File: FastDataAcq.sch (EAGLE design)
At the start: 223 parts, among them IC1 LT1963AEQ, IC2 FT230XQ, IC3 ADCMP553BRMZ, J1 MICRO-FIT_3.0_2POS_RA_SMD, J2 USB_MICROAB_SMT, J3 HEADER_0.1"_10P_2R_SMT, X1 87832-14, X2 SMA-142-0701-801/806, X3 SMA-142-0701-801/806, Y1 SI530-500, Y2 100MHz, Y3 DNP

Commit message: Digital layout complete.
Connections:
- removed net N3: U$2.IO_L12P_D1_MISO2_2
- removed net N4: U$2.IO_L12N_D2_MISO3_2
- removed net N5: U$2.IO_L13N_D10_2
- removed net N6: U$2.IO_L14P_D11_2
- removed net N7: U$2.IO_L14N_D12_2
- removed net N8: U$2.IO_L48P_D7_2
- removed net N9: U$2.IO_L48N_RDWR_B_VREF_2
- net 3V3: now also J3.P$9; no longer J3.P$1
- net FPGA_GPIO1: now also J3.P$4, U$2.IO_L48N_RDWR_B_VREF_2; no longer J3.P$9
- net FPGA_GPIO2: now also J3.P$2, U$2.IO_L48P_D7_2; no longer J3.P$8
- net FPGA_GPIO3: now also J3.P$1, U$2.IO_L14N_D12_2; no longer J3.P$7
- net FPGA_GPIO4: now also D3.CATHODE, J3.P$7, U$2.IO_L14P_D11_2; no longer J3.P$6
- net FPGA_GPIO5: now also J3.P$6, U$2.IO_L13N_D10_2; no longer J3.P$5
- net FPGA_GPIO6: now also D2.CATHODE, J3.P$5, U$2.IO_L12N_D2_MISO3_2; no longer D3.CATHODE, J3.P$4
- net FPGA_GPIO7: now also U$2.IO_L12P_D1_MISO2_2; no longer D2.CATHODE
- net GND: now also J3.P$10; no longer J3.P$2
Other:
- moved on the sheet: D2, D3, D4, R42, R43, R44

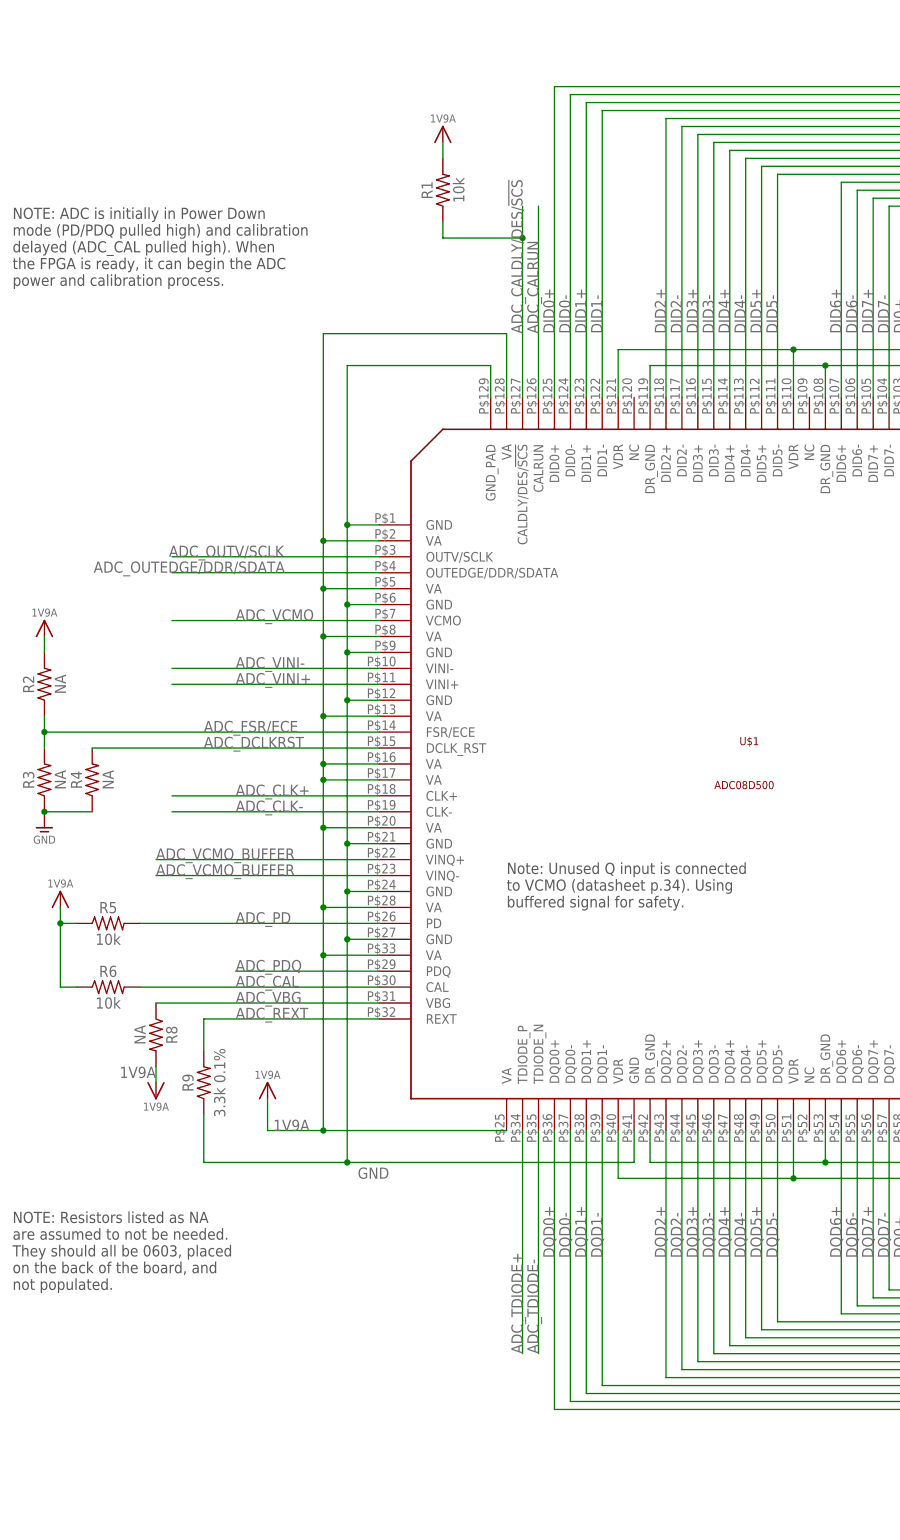
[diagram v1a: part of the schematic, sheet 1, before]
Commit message: PCB v0.1 done
Still need to fix a few things, but technically routing is done.
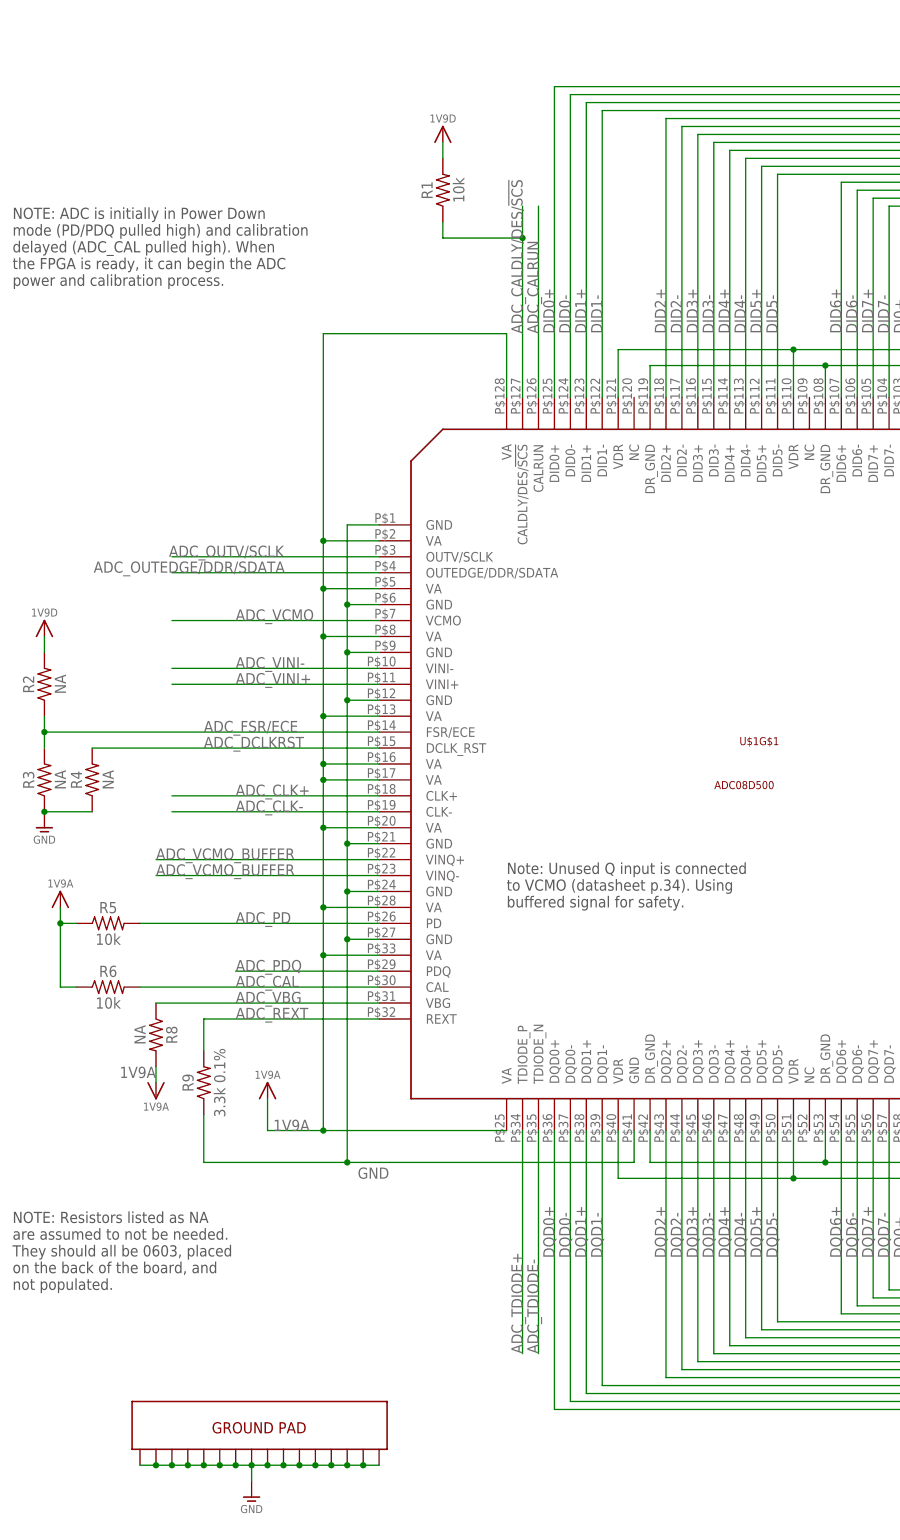
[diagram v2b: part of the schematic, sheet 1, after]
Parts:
- removed TP1, TP10, TP11, TP12, TP13, TP14, TP15, TP2, TP3, TP4, TP5, TP6, TP7, TP8, TP9: TPPAD1-13, testpad:TPPAD1-13
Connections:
- net 1V2: no longer TP1.TP
- net 1V8: no longer TP5.TP
- net 1V9: no longer TP7.TP
- net 1V9A: now also U$1G$1.VA@1, U$1G$1.VA@10, U$1G$1.VA@11, U$1G$1.VA@2, U$1G$1.VA@3, U$1G$1.VA@4, U$1G$1.VA@5, U$1G$1.VA@6, U$1G$1.VA@7, U$1G$1.VA@8, U$1G$1.VA@9; no longer R1.2, R2.2, U$1.VA@1, U$1.VA@10, U$1.VA@11, U$1.VA@2, U$1.VA@3, U$1.VA@4, U$1.VA@5, U$1.VA@6, U$1.VA@7, U$1.VA@8, U$1.VA@9
- net 1V9D: now also R1.2, R2.2, U$1G$1.VDR@1, U$1G$1.VDR@2, U$1G$1.VDR@3, U$1G$1.VDR@4, U$1G$1.VDR@5, U$1G$1.VDR@6, U$1G$1.VDR@7, U$1G$1.VDR@8; no longer U$1.VDR@1, U$1.VDR@2, U$1.VDR@3, U$1.VDR@4, U$1.VDR@5, U$1.VDR@6, U$1.VDR@7, U$1.VDR@8
- net 2V3_1V9PRE: no longer TP6.TP
- net 2V5: no longer TP9.TP
- net 2V8_2V5PRE: no longer TP8.TP
- net 3V3: no longer TP3.TP
- net 3V3A: no longer TP10.TP
- net 3V3S: no longer TP14.TP
- net 3V6_PRE3V3: no longer TP11.TP
- net ADC_CAL: now also U$1G$1.CAL; no longer U$1.CAL
- net ADC_CALDLY/DES/!SCS: now also U$1G$1.CALDLY/DES/!SCS; no longer U$1.CALDLY/DES/!SCS
- net ADC_CALRUN: now also U$1G$1.CALRUN; no longer U$1.CALRUN
- net ADC_CLK+: now also U$1G$1.CLK+; no longer U$1.CLK+
- net ADC_CLK-: now also U$1G$1.CLK-; no longer U$1.CLK-
- net ADC_DCLK+: now also U$1G$1.DCLK+; no longer U$1.DCLK+
- net ADC_DCLK-: now also U$1G$1.DCLK-; no longer U$1.DCLK-
- net ADC_DCLKRST: now also U$1G$1.DCLK_RST; no longer U$1.DCLK_RST
- net ADC_FSR/ECE: now also U$1G$1.FSR/ECE; no longer U$1.FSR/ECE
- net ADC_OUTEDGE/DDR/SDATA: now also U$1G$1.OUTEDGE/DDR/SDATA; no longer U$1.OUTEDGE/DDR/SDATA
- net ADC_OUTV/SCLK: now also U$1G$1.OUTV/SCLK; no longer U$1.OUTV/SCLK
- net ADC_PD: now also U$1G$1.PD; no longer U$1.PD
- net ADC_PDQ: now also U$1G$1.PDQ; no longer U$1.PDQ
- net ADC_REXT: now also U$1G$1.REXT; no longer U$1.REXT
- net ADC_TDIODE+: now also U$1G$1.TDIODE_P; no longer U$1.TDIODE_P
- net ADC_TDIODE-: now also U$1G$1.TDIODE_N; no longer U$1.TDIODE_N
- net ADC_VBG: now also U$1G$1.VBG; no longer U$1.VBG
- net ADC_VCMO: now also U$1G$1.VCMO; no longer U$1.VCMO
- net ADC_VCMO_BUFFER: now also U$1G$1.VINQ+, U$1G$1.VINQ-; no longer U$1.VINQ+, U$1.VINQ-
- net ADC_VINI+: now also U$1G$1.VINI+; no longer U$1.VINI+
- net ADC_VINI-: now also U$1G$1.VINI-; no longer U$1.VINI-
- net DI0+: now also U$1G$1.DI0+; no longer U$1.DI0+
- net DI0-: now also U$1G$1.DI0-; no longer U$1.DI0-
- net DI1+: now also U$1G$1.DI1+; no longer U$1.DI1+
- net DI1-: now also U$1G$1.DI1-; no longer U$1.DI1-
- net DI2+: now also U$1G$1.DI2+; no longer U$1.DI2+
- net DI2-: now also U$1G$1.DI2-; no longer U$1.DI2-
- net DI3+: now also U$1G$1.DI3+; no longer U$1.DI3+
- net DI3-: now also U$1G$1.DI3-; no longer U$1.DI3-
- net DI4+: now also U$1G$1.DI4+; no longer U$1.DI4+
- net DI4-: now also U$1G$1.DI4-; no longer U$1.DI4-
- net DI5+: now also U$1G$1.DI5+; no longer U$1.DI5+
- net DI5-: now also U$1G$1.DI5-; no longer U$1.DI5-
- net DI6+: now also U$1G$1.DI6+; no longer U$1.DI6+
- net DI6-: now also U$1G$1.DI6-; no longer U$1.DI6-
- net DI7+: now also U$1G$1.DI7+; no longer U$1.DI7+
- net DI7-: now also U$1G$1.DI7-; no longer U$1.DI7-
- net DID0+: now also U$1G$1.DID0+; no longer U$1.DID0+
- net DID0-: now also U$1G$1.DID0-; no longer U$1.DID0-
- net DID1+: now also U$1G$1.DID1+; no longer U$1.DID1+
- net DID1-: now also U$1G$1.DID1-; no longer U$1.DID1-
- net DID2+: now also U$1G$1.DID2+; no longer U$1.DID2+
- net DID2-: now also U$1G$1.DID2-; no longer U$1.DID2-
- net DID3+: now also U$1G$1.DID3+; no longer U$1.DID3+
- net DID3-: now also U$1G$1.DID3-; no longer U$1.DID3-
- net DID4+: now also U$1G$1.DID4+; no longer U$1.DID4+
- net DID4-: now also U$1G$1.DID4-; no longer U$1.DID4-
- net DID5+: now also U$1G$1.DID5+; no longer U$1.DID5+
- net DID5-: now also U$1G$1.DID5-; no longer U$1.DID5-
- net DID6+: now also U$1G$1.DID6+; no longer U$1.DID6+
- net DID6-: now also U$1G$1.DID6-; no longer U$1.DID6-
- net DID7+: now also U$1G$1.DID7+; no longer U$1.DID7+
- net DID7-: now also U$1G$1.DID7-; no longer U$1.DID7-
- net DQ0+: now also U$1G$1.DQ0+; no longer U$1.DQ0+
- net DQ0-: now also U$1G$1.DQ0-; no longer U$1.DQ0-
- net DQ1+: now also U$1G$1.DQ1+; no longer U$1.DQ1+
- net DQ1-: now also U$1G$1.DQ1-; no longer U$1.DQ1-
- net DQ2+: now also U$1G$1.DQ2+; no longer U$1.DQ2+
- net DQ2-: now also U$1G$1.DQ2-; no longer U$1.DQ2-
- net DQ3+: now also U$1G$1.DQ3+; no longer U$1.DQ3+
- net DQ3-: now also U$1G$1.DQ3-; no longer U$1.DQ3-
- net DQ4+: now also U$1G$1.DQ4+; no longer U$1.DQ4+
- net DQ4-: now also U$1G$1.DQ4-; no longer U$1.DQ4-
- net DQ5+: now also U$1G$1.DQ5+; no longer U$1.DQ5+
- net DQ5-: now also U$1G$1.DQ5-; no longer U$1.DQ5-
- net DQ6+: now also U$1G$1.DQ6+; no longer U$1.DQ6+
- net DQ6-: now also U$1G$1.DQ6-; no longer U$1.DQ6-
- net DQ7+: now also U$1G$1.DQ7+; no longer U$1.DQ7+
- net DQ7-: now also U$1G$1.DQ7-; no longer U$1.DQ7-
- net DQD0+: now also U$1G$1.DQD0+; no longer U$1.DQD0+
- net DQD0-: now also U$1G$1.DQD0-; no longer U$1.DQD0-
- net DQD1+: now also U$1G$1.DQD1+; no longer U$1.DQD1+
- net DQD1-: now also U$1G$1.DQD1-; no longer U$1.DQD1-
- net DQD2+: now also U$1G$1.DQD2+; no longer U$1.DQD2+
- net DQD2-: now also U$1G$1.DQD2-; no longer U$1.DQD2-
- net DQD3+: now also U$1G$1.DQD3+; no longer U$1.DQD3+
- net DQD3-: now also U$1G$1.DQD3-; no longer U$1.DQD3-
- net DQD4+: now also U$1G$1.DQD4+; no longer U$1.DQD4+
- net DQD4-: now also U$1G$1.DQD4-; no longer U$1.DQD4-
- net DQD5+: now also U$1G$1.DQD5+; no longer U$1.DQD5+
- net DQD5-: now also U$1G$1.DQD5-; no longer U$1.DQD5-
- net DQD6+: now also U$1G$1.DQD6+; no longer U$1.DQD6+
- net DQD6-: now also U$1G$1.DQD6-; no longer U$1.DQD6-
- net DQD7+: now also U$1G$1.DQD7+; no longer U$1.DQD7+
- net DQD7-: now also U$1G$1.DQD7-; no longer U$1.DQD7-
- net FPGA_DONE: no longer TP13.TP
- net FPGA_INITB: no longer TP12.TP
- net GND: now also U$1G$1.DR_GND@1, U$1G$1.DR_GND@2, U$1G$1.DR_GND@3, U$1G$1.DR_GND@4, U$1G$1.DR_GND@5, U$1G$1.DR_GND@6, U$1G$1.DR_GND@7, U$1G$1.DR_GND@8, U$1G$1.GND@1, U$1G$1.GND@2, U$1G$1.GND@3, U$1G$1.GND@4, U$1G$1.GND@5, U$1G$1.GND@6, U$1G$1.GND@7, U$1G$1.GND@8, U$1G$2.GND@0, U$1G$2.GND@1, U$1G$2.GND@10, U$1G$2.GND@11, U$1G$2.GND@12, U$1G$2.GND@13, U$1G$2.GND@14, U$1G$2.GND@15, U$1G$2.GND@2, U$1G$2.GND@3, U$1G$2.GND@4, U$1G$2.GND@5, U$1G$2.GND@6, U$1G$2.GND@7, U$1G$2.GND@8, U$1G$2.GND@9; no longer U$1.DR_GND@1, U$1.DR_GND@2, U$1.DR_GND@3, U$1.DR_GND@4, U$1.DR_GND@5, U$1.DR_GND@6, U$1.DR_GND@7, U$1.DR_GND@8, U$1.GND@1, U$1.GND@2, U$1.GND@3, U$1.GND@4, U$1.GND@5, U$1.GND@6, U$1.GND@7, U$1.GND@8, U$1.GND_PAD
- net PGOOD: no longer TP2.TP
- net S_TEMP: no longer TP4.TP
- net TRIG_REF: no longer TP15.TP

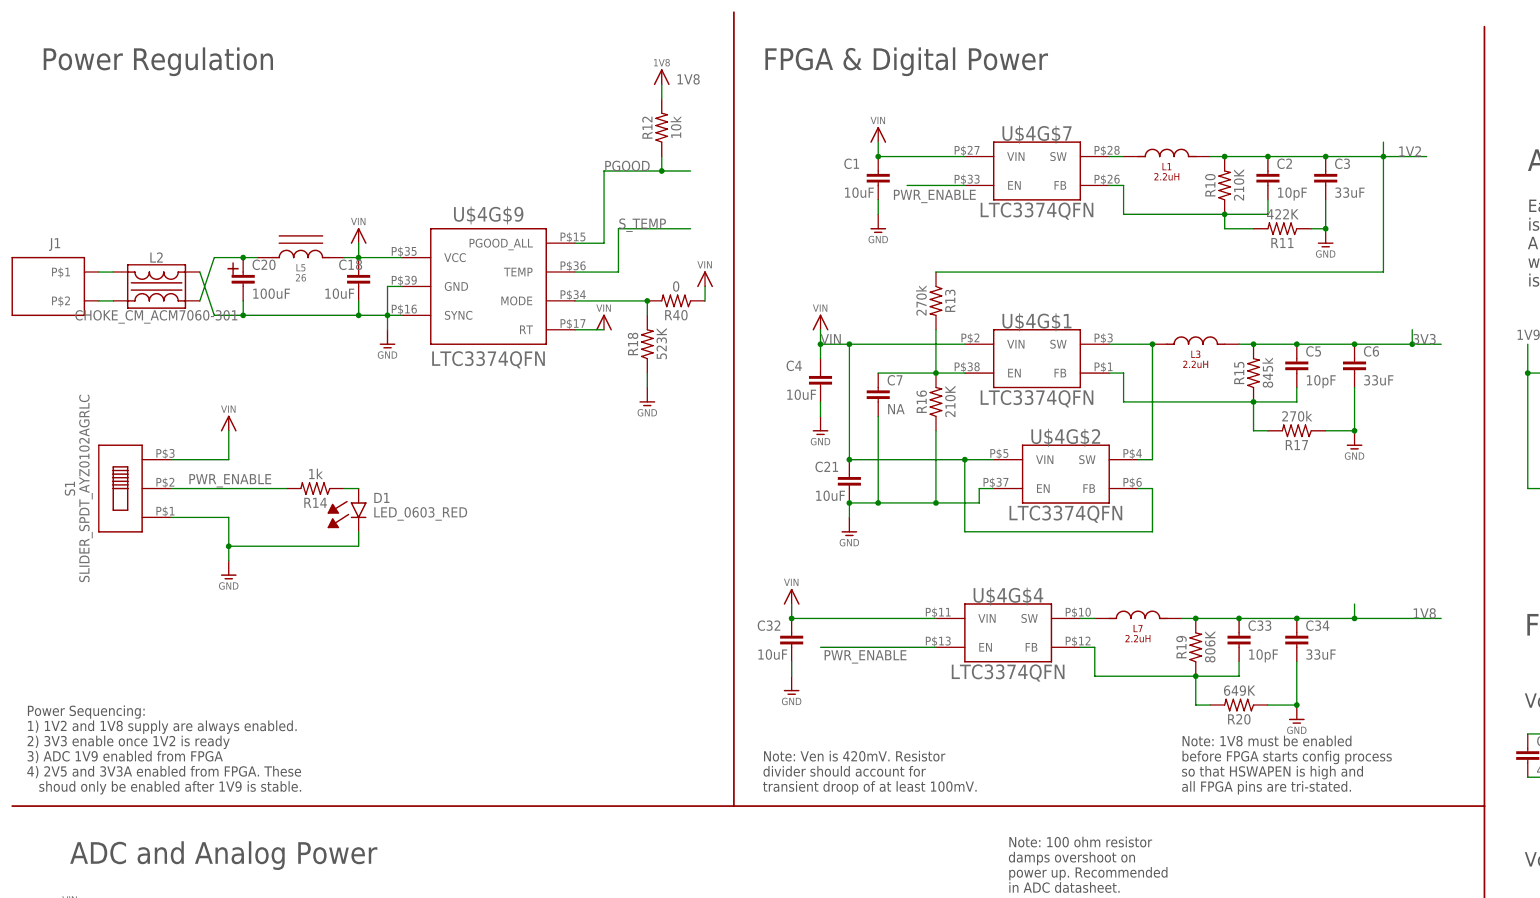
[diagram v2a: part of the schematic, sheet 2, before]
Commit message: Several changes
There are several changes after discussing the design with Grant
Elliott. Most notably is the addition of a On/Off Debounce Latch IC.
Additionally the CTS is now connected to the FPGA to force the packet to
be sent.
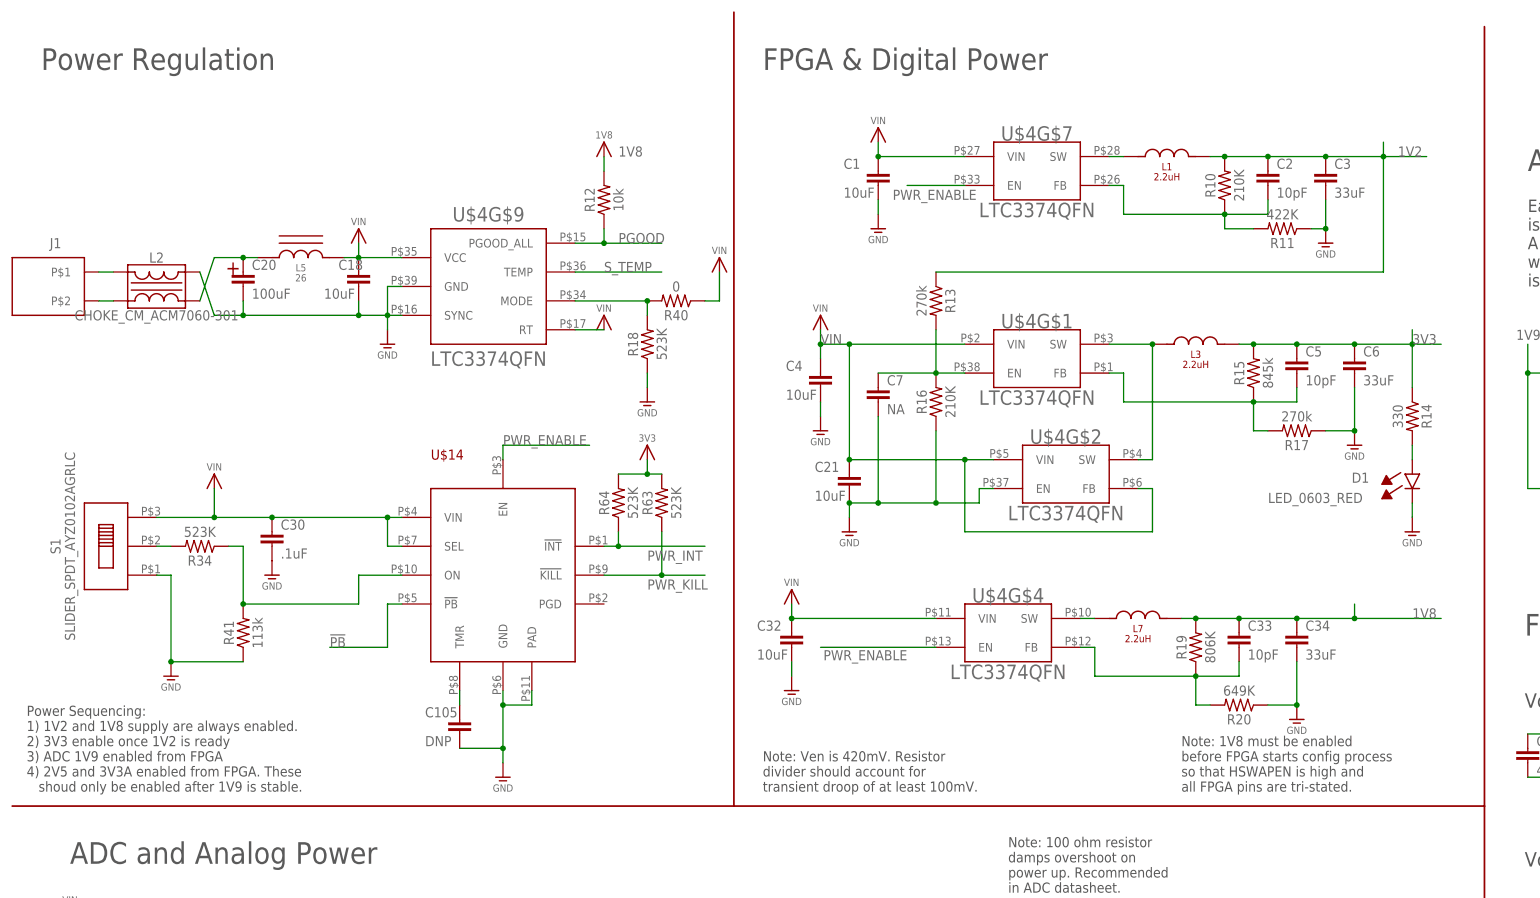
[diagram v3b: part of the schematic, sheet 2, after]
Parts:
- added C105: DNP, rcl:C-EUC0603
- added C30: .1uF, Schuyler:CAPACITOR0204_REVERSE
- added R34, R63, R64: 523K, rcl:R-US_R0201
- added R41: 113k, rcl:R-US_R0201
- added U$14: LTC2955-1, Schuyler:LTC2955-1
- R14: value 1k -> 330; MANPARTNUMBER (none) -> RC0603J331CS; MANUFACTURER (none) -> Samsung Electro-Mechanics America, Inc; PARTNUMBER 1276-3797-1-ND -> 1276-3787-1-ND
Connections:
- removed net FPGA_GPIO4: D3.CATHODE, J3.P$7, U$2.IO_L14P_D11_2
- removed net FPGA_GPIO5: D4.CATHODE, J3.P$6, U$2.IO_L13N_D10_2
- removed net FPGA_GPIO6: D2.CATHODE, J3.P$5, U$2.IO_L12N_D2_MISO3_2
- removed net N$9: D1.ANODE, R14.1
- new net !PB: U$14.!PB
- new net FPGA_CTS: D3.CATHODE, IC2.!CTS, U$2.IO_L14P_D11_2
- new net N$1: D1.ANODE, R14.2
- new net N$12: R34.1, R41.2, U$14.ON
- new net N$17: C105.1, U$14.TMR
- new net N$6: R34.2, S1.P$2
- new net PWR_INT: R64.1, U$14.!INT, U$2.IO_L13N_D10_2
- new net PWR_KILL: R63.1, U$14.!KILL, U$2.IO_L12N_D2_MISO3_2
- net 3V3: now also R14.1, R63.2, R64.2
- net GND: now also C105.2, C30.2, R41.1, U$14.GND, U$14.PAD
- net PWR_ENABLE: now also U$14.EN; no longer R14.2, S1.P$2
- net VIN: now also C30.1, U$14.SEL, U$14.VIN
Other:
- note removed: "Note: Current limiting resistors may not be necessary."
- moved on the sheet: C101, D1, L13, R12, R14, S1

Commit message: PCB Power Layer and Other Fixes
Finalized the FPGA GPIO Pins. Fixed power layer so that all spacing is
equal and entire layer covered. Other cosmetic fixes.
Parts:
- removed J3: HEADER_0.1"_10P_2R_SMT, Schuyler:HEADER_0.1"_10P_2R_SMT
- added U$95: HEADER_0.1"_8P_2R_SMT, Schuyler:HEADER_0.1"_8P_2R_SMT
- R2, R3, R4, R8: value NA -> DNP
- R40: value 0 -> DNP
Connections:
- net ADC_DCLK+ renamed ADC_DCLK_P
- net ADC_DCLK- renamed ADC_DCLK_N
- net DI2+ renamed DI2_P
- net DI2- renamed DI2_N
- net DI3+ renamed DI3_P
- net DI3- renamed DI3_N
- net DI4+ renamed DI4_P
- net DI4- renamed DI4_N
- net DI5+ renamed DI5_P
- net DI5- renamed DI5_N
- net DI6+ renamed DI6_P
- net DI6- renamed DI6_N
- net DI7+ renamed DI7_P
- net DI7- renamed DI7_N
- net DQ3+ renamed DQ3_N
- net DQ3- renamed DQ3_P
- net DQ4+ renamed DQ4_N
- net DQ4- renamed DQ4_P
- net DQ5+ renamed DQ5_N
- net DQ5- renamed DQ5_P
- net DQ6+ renamed DQ6_N
- net DQ6- renamed DQ6_P
- net DQ7+ renamed DQ7_N
- net DQ7- renamed DQ7_P
- removed net FPGA_GPIO7: J3.P$3, U$2.IO_L12P_D1_MISO2_2
- new net FPGA_GPIO4: D2.CATHODE, U$2.IO_L12P_D1_MISO2_2, U$95.P$3
- net !PB: now also U$95.P$5
- net 3V3: now also U$95.P$7; no longer J3.P$9
- net FPGA_CTS: no longer D3.CATHODE
- net FPGA_GPIO1: now also D4.CATHODE, U$95.P$4; no longer J3.P$4
- net FPGA_GPIO2: now also U$95.P$2; no longer J3.P$2
- net FPGA_GPIO3: now also D3.CATHODE, U$95.P$1; no longer J3.P$1
- net GND: now also U$95.P$8; no longer J3.P$10
- net S_TEMP: now also U$95.P$6
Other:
- note added: "NOTE: Bypassing for clock discussed in SILabs Docs."
- note removed: "NOTE: Bypassing for clock discussed in SILabs Docs. Changge inductor to Venkel version."
- note removed: "NOTE: Include pull-up but DNP."
- moved on the sheet: C76, C77, C78, C80, C81, L11, R5, R6, R8, R9
